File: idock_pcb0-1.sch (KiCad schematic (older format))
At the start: 9 parts, among them J1 entrada, U1 ATmega32A-PU, Y1 8mhz

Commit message: add conections to ipod pcb
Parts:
- removed J1: entrada, Connector_PinHeader_2.00mm:PinHeader_1x02_P2.00mm_Vertical, symbol Connector:Screw_Terminal_01x02
- removed J?: Screw_Terminal_01x05, symbol Connector:Screw_Terminal_01x05
- added J1: Barrel_Jack_Switch, Connector_BarrelJack:BarrelJack_Wuerth_6941xx301002, symbol Connector:Barrel_Jack_Switch
- added J2: bluetooth-dock, Connector_PinSocket_2.54mm:PinSocket_1x11_P2.54mm_Vertical, symbol Connector:Screw_Terminal_01x11
- added Q1: BC548, Package_TO_SOT_THT:TO-92_Inline_Wide, symbol Transistor_BJT:BC548
- added R3: 10k, Resistor_THT:R_Axial_DIN0207_L6.3mm_D2.5mm_P7.62mm_Horizontal, symbol Device:R
- added R4: 47k, Resistor_THT:R_Axial_DIN0207_L6.3mm_D2.5mm_P7.62mm_Horizontal, symbol Device:R
- added SW1: Reset, Button_Switch_THT:SW_PUSH_6mm, symbol Switch:SW_Push
- R1, R2: footprint Resistor_THT:R_Axial_DIN0309_L9.0mm_D3.2mm_P12.70mm_Horizontal -> Resistor_THT:R_Axial_DIN0207_L6.3mm_D2.5mm_P7.62mm_Horizontal
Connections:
- wire segments 37 -> 67
- no-connect marks 31 -> 32
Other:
- note added: "BT-GND"
- note added: "BT-RXD"
- note added: "BT-TXD"
- note added: "BT-VCC"
- note added: "Dock-GND"
- note added: "Dock-RX"
- note added: "Dock-TX\n"
- note added: "Dock-VCC"
- note added: "Dock-audio-GND"
- note added: "Dock-audio-L"
- note added: "Dock-audio-R"
- moved on the sheet: C1, C2, D1, R1, R2, U1, Y1

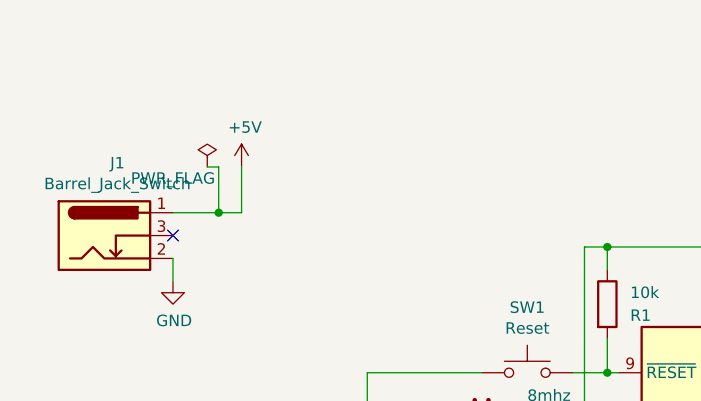
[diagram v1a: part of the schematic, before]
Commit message: add labels to PCB
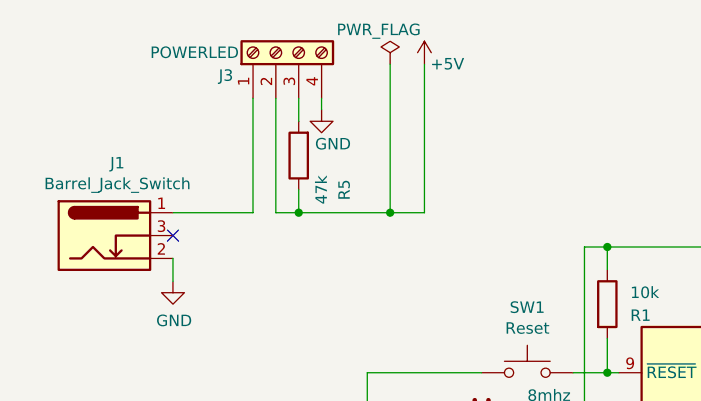
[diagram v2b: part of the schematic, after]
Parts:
- added J3: POWERLED, Connector_PinSocket_2.54mm:PinSocket_1x04_P2.54mm_Vertical, symbol Connector:Screw_Terminal_01x04
- added R5: 47k, Resistor_THT:R_Axial_DIN0207_L6.3mm_D2.5mm_P7.62mm_Horizontal, symbol Device:R
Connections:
- net +5V: now also J3.2 (Pin_2), R5.1; no longer J1.1
- net GND: now also J3.4 (Pin_4)
- new net: J1.1, J3.1 (Pin_1)
- new net: J3.3 (Pin_3), R5.2
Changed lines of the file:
@@
 	1    0    0    -1
 $EndComp
-Wire Wire Line
-	2150 1350 2350 1350
-Wire Wire Line
-	2350 1350 2450 1350
-Connection ~ 2350 1350
-Wire Wire Line
-	2350 1150 2300 1150
-Wire Wire Line
-	2350 1350 2350 1150
 $Comp
 L power:PWR_FLAG #FLG01
 U 1 1 5F6FEFE5
-P 2300 1150
-F 0 "#FLG01" H 2300 1225 50  0001 C CNN
-F 1 "PWR_FLAG" H 2150 1100 50  0000 C CNN
-F 2 "" H 2300 1150 50  0001 C CNN
-F 3 "~" H 2300 1150 50  0001 C CNN
-	1    2300 1150
-	1    0    0    -1
-$EndComp
-$Comp
-L power:+5V #PWR05
-U 1 1 5F6D56BF
-P 2450 1150
-F 0 "#PWR05" H 2450 1000 50  0001 C CNN
-F 1 "+5V" H 2465 1323 50  0000 C CNN
-F 2 "" H 2450 1150 50  0001 C CNN
-F 3 "" H 2450 1150 50  0001 C CNN
-	1    2450 1150
-	1    0    0    -1
-$EndComp
-Wire Wire Line
-	2450 1350 2450 1150
+P 3100 700
+F 0 "#FLG01" H 3100 775 50  0001 C CNN
+F 1 "PWR_FLAG" H 3050 850 50  0000 C CNN
+F 2 "" H 3100 700 50  0001 C CNN
+F 3 "~" H 3100 700 50  0001 C CNN
+	1    3100 700
+	1    0    0    -1
+$EndComp
 $Comp
 L power:GND #PWR06
@@
 Text Notes 8700 5500 0    50   ~ 0
 BT-RXD
+$Comp
+L power:+5V #PWR05
+U 1 1 5F6D56BF
+P 3250 700
+F 0 "#PWR05" H 3250 550 50  0001 C CNN
+F 1 "+5V" H 3350 700 50  0000 C CNN
+F 2 "" H 3250 700 50  0001 C CNN
+F 3 "" H 3250 700 50  0001 C CNN
+	1    3250 700
+	1    0    0    -1
+$EndComp
+$Comp
+L Connector:Screw_Terminal_01x04 J3
+U 1 1 5F7A8A08
+P 2600 650
+F 0 "J3" V 2500 900 50  0000 R CNN
+F 1 "POWERLED" V 2600 1200 50  0000 R CNN
+F 2 "Connector_PinSocket_2.54mm:PinSocket_1x04_P2.54mm_Vertical" H 2600 650 50  0001 C CNN
+F 3 "~" H 2600 650 50  0001 C CNN
+	1    2600 650
+	0    -1   -1   0
+$EndComp
+$Comp
+L Device:R R5
+U 1 1 5F7B018C
+P 2700 1100
+F 0 "R5" V 2500 1250 50  0000 C CNN
+F 1 "47k" V 2600 1250 50  0000 C CNN
+F 2 "Resistor_THT:R_Axial_DIN0207_L6.3mm_D2.5mm_P7.62mm_Horizontal" V 2630 1100 50  0001 C CNN
+F 3 "~" H 2700 1100 50  0001 C CNN
+	1    2700 1100
+	-1   0    0    1
+$EndComp
+Wire Wire Line
+	3250 1350 3250 700
+Wire Wire Line
+	3100 700  3100 1350
+Connection ~ 3100 1350
+Wire Wire Line
+	3100 1350 3250 1350
+Wire Wire Line
+	2700 850  2700 950
+Wire Wire Line
+	2700 1250 2700 1350
+Connection ~ 2700 1350
+Wire Wire Line
+	2700 1350 3100 1350
+$Comp
+L power:GND #PWR08
+U 1 1 5F7D410A
+P 2800 900
+F 0 "#PWR08" H 2800 650 50  0001 C CNN
+F 1 "GND" H 2850 750 50  0000 C CNN
+F 2 "" H 2800 900 50  0001 C CNN
+F 3 "" H 2800 900 50  0001 C CNN
+	1    2800 900
+	1    0    0    -1
+$EndComp
+Wire Wire Line
+	2800 850  2800 900
+Wire Wire Line
+	2600 1350 2700 1350
+Wire Wire Line
+	2500 1350 2150 1350
+Wire Wire Line
+	2500 850  2500 1350
+Wire Wire Line
+	2600 850  2600 1350
 $EndSCHEMATC

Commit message: retomando PCB
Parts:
- D1: value LED BLUE -> LED BLUE DATA RX
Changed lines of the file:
@@
 P 5950 5650
 F 0 "D1" V 5989 5532 50  0000 R CNN
-F 1 "LED BLUE" V 5898 5532 50  0000 R CNN
+F 1 "LED BLUE DATA RX" V 5898 5532 50  0000 R CNN
 F 2 "LED_THT:LED_D5.0mm_Clear" H 5950 5650 50  0001 C CNN
 F 3 "~" H 5950 5650 50  0001 C CNN

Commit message: pcb with correct size and holes
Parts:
- added J4: Conn_Coaxial_x2, symbol Connector:Conn_Coaxial_x2
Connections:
- net at J2.1 (Pin_1): now also J4.3 (EXT)
- net at J2.2 (Pin_2): now also J4.2 (IN2)
- net at J2.3 (Pin_3): now also J4.1 (IN1)
- no-connect marks 32 -> 29
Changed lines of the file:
@@
 Wire Wire Line
 	8300 5300 8400 5300
-NoConn ~ 8400 4700
-NoConn ~ 8400 4600
-NoConn ~ 8400 4500
 Wire Wire Line
 	5300 4750 8000 4750
@@
 Wire Wire Line
 	2600 850  2600 1350
+Wire Wire Line
+	8350 4700 8400 4700
+Wire Wire Line
+	8350 4650 8350 4700
+Wire Wire Line
+	7900 4650 8350 4650
+Wire Wire Line
+	7900 4250 7900 4650
+Wire Wire Line
+	8300 4050 8400 4050
+Wire Wire Line
+	8400 4050 8400 4500
+Wire Wire Line
+	8100 4600 8400 4600
+Wire Wire Line
+	8100 4250 8100 4600
+$Comp
+L Connector:Conn_Coaxial_x2 J4
+U 1 1 60D9751E
+P 8000 4050
+F 0 "J4" V 8237 3979 50  0000 C CNN
+F 1 "Conn_Coaxial_x2" V 8146 3979 50  0000 C CNN
+F 2 "" H 8000 3950 50  0001 C CNN
+F 3 " ~" H 8000 3950 50  0001 C CNN
+	1    8000 4050
+	0    -1   -1   0
+$EndComp
 $EndSCHEMATC

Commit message: add footprints PJRAN2X1UO2
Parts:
- removed J4: Conn_Coaxial_x2, symbol Connector:Conn_Coaxial_x2
- added J4: PJRAN2X1U02, footprints:SWITCHCRAFT_PJRAN2X1U02, symbol PJRAN2X1U02:PJRAN2X1U02
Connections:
- net at J2.1 (Pin_1): now also J4.1A, J4.1B
- net at J2.2 (Pin_2): now also J4.2B
- net at J2.3 (Pin_3): now also J4.2A
- no-connect marks 29 -> 31
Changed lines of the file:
@@
 Wire Wire Line
 	2600 850  2600 1350
+$Comp
+L PJRAN2X1U02:PJRAN2X1U02 J4
+U 1 1 60DF5E40
+P 9050 3300
+F 0 "J4" H 8796 3255 50  0000 R CNN
+F 1 "PJRAN2X1U02" H 8796 3346 50  0000 R CNN
+F 2 "footprints:SWITCHCRAFT_PJRAN2X1U02" H 9050 3300 50  0001 L BNN
+F 3 "" H 9050 3300 50  0001 L BNN
+F 4 "Manufacturer Recommendations" H 9050 3300 50  0001 L BNN "STANDARD"
+F 5 "13.5 mm" H 9050 3300 50  0001 L BNN "MAXIMUM_PACKAGE_HEIGHT"
+F 6 "Switchcraft" H 9050 3300 50  0001 L BNN "MANUFACTURER"
+F 7 "A" H 9050 3300 50  0001 L BNN "PARTREV"
+	1    9050 3300
+	-1   0    0    1
+$EndComp
+$Comp
+L PJRAN2X1U02:PJRAN2X1U02 J4
+U 2 1 60DF6EE1
+P 9050 3650
+F 0 "J4" H 8796 3605 50  0000 R CNN
+F 1 "PJRAN2X1U02" H 8796 3696 50  0000 R CNN
+F 2 "footprints:SWITCHCRAFT_PJRAN2X1U02" H 9050 3650 50  0001 L BNN
+F 3 "" H 9050 3650 50  0001 L BNN
+F 4 "Manufacturer Recommendations" H 9050 3650 50  0001 L BNN "STANDARD"
+F 5 "13.5 mm" H 9050 3650 50  0001 L BNN "MAXIMUM_PACKAGE_HEIGHT"
+F 6 "Switchcraft" H 9050 3650 50  0001 L BNN "MANUFACTURER"
+F 7 "A" H 9050 3650 50  0001 L BNN "PARTREV"
+	2    9050 3650
+	-1   0    0    1
+$EndComp
 Wire Wire Line
-	8350 4700 8400 4700
+	8400 4600 8350 4600
 Wire Wire Line
-	8350 4650 8350 4700
+	8350 4600 8350 3750
 Wire Wire Line
-	7900 4650 8350 4650
+	8350 3750 8750 3750
 Wire Wire Line
-	7900 4250 7900 4650
+	8400 4700 8350 4700
 Wire Wire Line
-	8300 4050 8400 4050
+	8350 4700 8350 4650
 Wire Wire Line
-	8400 4050 8400 4500
+	8350 4650 8300 4650
 Wire Wire Line
-	8100 4600 8400 4600
+	8300 4650 8300 3400
 Wire Wire Line
-	8100 4250 8100 4600
-$Comp
-L Connector:Conn_Coaxial_x2 J4
-U 1 1 60D9751E
-P 8000 4050
-F 0 "J4" V 8237 3979 50  0000 C CNN
-F 1 "Conn_Coaxial_x2" V 8146 3979 50  0000 C CNN
-F 2 "" H 8000 3950 50  0001 C CNN
-F 3 " ~" H 8000 3950 50  0001 C CNN
-	1    8000 4050
-	0    -1   -1   0
-$EndComp
+	8300 3400 8750 3400
+Wire Wire Line
+	8400 4500 8400 3550
+Wire Wire Line
+	8400 3200 8750 3200
+Wire Wire Line
+	8400 3550 8750 3550
+Connection ~ 8400 3550
+Wire Wire Line
+	8400 3550 8400 3200
+NoConn ~ 8750 3650
+NoConn ~ 8750 3300
 $EndSCHEMATC

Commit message: printing tests
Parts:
- removed J2: bluetooth-dock, Connector_PinSocket_2.54mm:PinSocket_1x11_P2.54mm_Vertical, symbol Connector:Screw_Terminal_01x11
- added J2: dock, Connector_PinSocket_2.54mm:PinSocket_1x07_P2.54mm_Vertical, symbol Connector:Screw_Terminal_01x07
- added J5: Bluetooth Module, Connector_PinSocket_2.54mm:PinSocket_1x04_P2.54mm_Vertical, symbol Connector:Screw_Terminal_01x04
- added TP1, TP2, TP3, TP4, TP5: TestPoint, TestPoint:TestPoint_Pad_D1.5mm, symbol Connector:TestPoint
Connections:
- net +5V: now also J2.7 (Pin_7), J5.1 (Pin_1)
- net GND: now also J2.6 (Pin_6), J5.2 (Pin_2), TP2.1
- net at U1.14 (PD0): now also J2.5 (Pin_5), J5.3 (Pin_3), TP5.1
- net at Q1.1 (C), U1.15 (PD1): now also J2.4 (Pin_4), TP4.1
- net at R1.2, SW1.2, U1.9 (~RESET): now also TP3.1
- net at Q1.3 (E), R4.2: now also J5.4 (Pin_4)
- net at J1.1, J3.1 (Pin_1): now also TP1.1
- net at J4.1A, J4.1B: now also J2.1 (Pin_1)
- net at J4.2B: now also J2.2 (Pin_2)
- net at J4.2A: now also J2.3 (Pin_3)
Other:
- moved on the sheet: C1, C2, D1, J1, J3, J4A, J4B, Q1, R1, R2, R3, R4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
